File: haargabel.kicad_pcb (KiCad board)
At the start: 4 copper layers, 159 x 36 mm, 95 parts, among them J1 SWD, J2 USB_B_Micro, J3 Conn_01x03, SW1 SKRKAEE020, U1 ATSAML21E15B-MUT, U2 MCP73831-2-OT, U3 TPS79330-EP, U4 MPU-6050, U5 TPS22929D

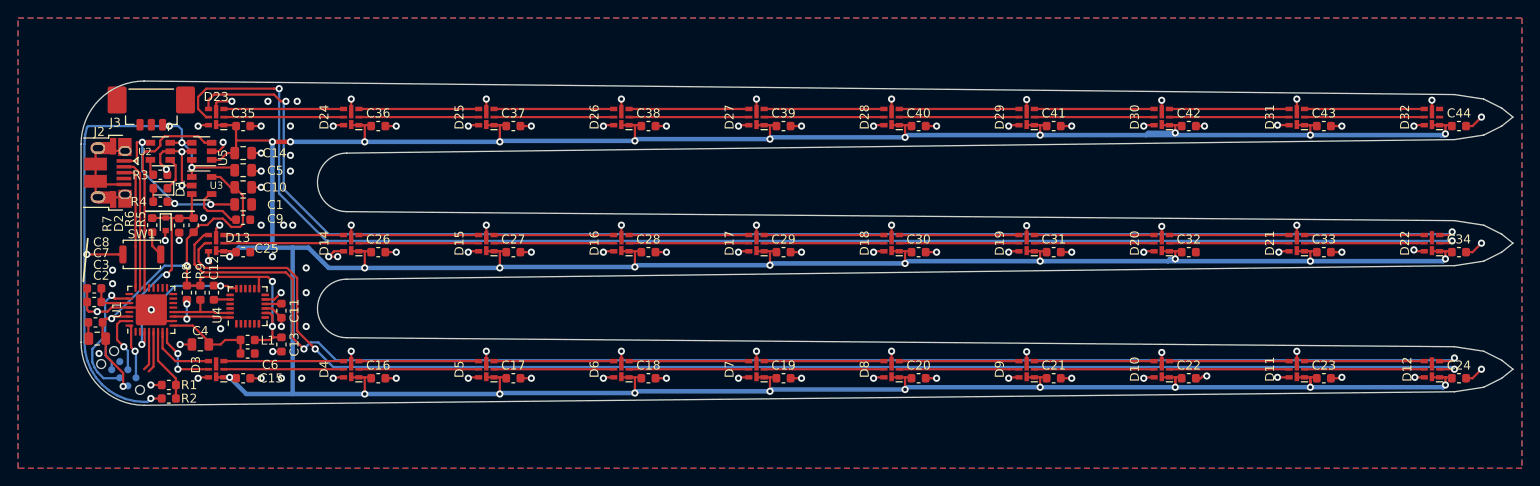
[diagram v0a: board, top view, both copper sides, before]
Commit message: Use a different MCU to make programming easier
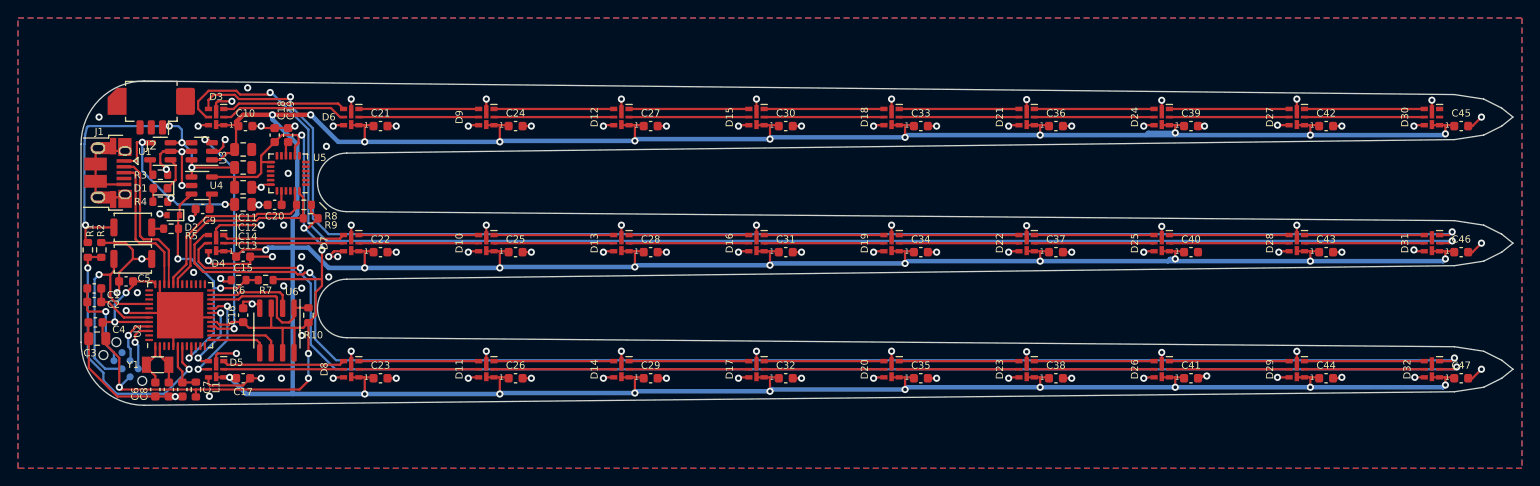
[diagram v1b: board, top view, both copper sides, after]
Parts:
- removed the C4 at (123.2, 79.2)
- removed the U1 at (117.8, 75.4)
- added C16: 100n, Capacitor_SMD:C_0603_1608Metric, F.Cu at (128.0, 76.0)
- added C5: 100n, Capacitor_SMD:C_0603_1608Metric, F.Cu at (115.0, 72.2)
- added C6: 100n, Capacitor_SMD:C_0603_1608Metric, F.Cu at (118.2, 84.2)
- added C8: 100n, Capacitor_SMD:C_0603_1608Metric, F.Cu at (119.8, 84.2)
- added R10: 10k, Resistor_SMD:R_0603_1608Metric, F.Cu at (135.2, 76.0)
- added SW2: SKRKAEE020, Button_Switch_SMD:SW_Push_SPST_NO_Alps_SKRK, F.Cu at (115.8, 69.8)
- added U2: ATSAMD21G18A-M, Package_DFN_QFN:QFN-48-1EP_7x7mm_P0.5mm_EP5.15x5.15mm, F.Cu at (121.0, 76.0)
- added U6: AT25SF081-SSHD-X, Package_SO:SOIC-8_3.9x4.9mm_P1.27mm, F.Cu at (131.8, 77.7)
- added Y1: Crystal, Crystal:Crystal_SMD_3215-2Pin_3.2x1.5mm, F.Cu at (118.5, 81.5)
- J2: renamed from J3; footprint Connector_Molex:Molex_PicoBlade_53398-0371_1x03-1MP_P1.25mm_Vertical -> Connector_Molex:Molex_PicoBlade_53261-0371_1x03-1MP_P1.25mm_Horizontal
- moved C18 23.3 mm to (131.5, 56.0), turned to 90 degrees
- moved C19 19.5 mm to (133.0, 56.0), turned to 90 degrees
- moved R1 18.8 mm to (110.8, 68.8), turned to -90 degrees
- moved R2 16.8 mm to (112.2, 68.8), turned to 90 degrees
- moved R9 16.0 mm to (135.5, 65.2), turned to 180 degrees
- moved U5 15.4 mm to (133.0, 60.2), turned to 180 degrees
- moved R8 15.1 mm to (134.8, 63.8), turned to 180 degrees
- moved C20 11.9 mm to (131.5, 63.8), turned to 180 degrees
- moved R7 10.1 mm to (130.5, 72.1), turned to 180 degrees
- moved R6 8.96 mm to (127.5, 72.1), turned to 180 degrees
- moved C7 8.28 mm to (121.2, 84.2), turned to -90 degrees
- moved L1 7.96 mm to (122.8, 84.2), turned to 90 degrees
- moved C9 4.66 mm to (123.5, 64.2), turned to 0 degrees
- moved SW1 3.16 mm to (115.8, 66.2)
- moved R5 2.14 mm to (120.0, 66.4), turned to 0 degrees
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- renumbered C8 to C1, C35 to C10, C14 to C11, C5 to C12, C1 to C13, C10 to C14, C25 to C15, C15 to C17, C13 to C18, C11 to C19, C7 to C2, C12 to C20, C36 to C21, C26 to C22, C16 to C23, C37 to C24, C27 to C25, C17 to C26, C38 to C27, C18 to C29, C2 to C3, C39 to C30, C29 to C31, C19 to C32, C40 to C33, C30 to C34, C20 to C35, C41 to C36, C31 to C37, C21 to C38, C42 to C39, C3 to C4, C32 to C40, C22 to C41, C43 to C42, C33 to C43, C23 to C44, C44 to C45, C34 to C46, C24 to C47, C6 to C7, D15 to D10, D5 to D11, D26 to D12, D16 to D13, D6 to D14, D27 to D15, D17 to D16, D7 to D17, D28 to D18, D18 to D19, D8 to D20, D29 to D21, D19 to D22, D9 to D23, D30 to D24, D20 to D25, D10 to D26, D31 to D27, D21 to D28, D11 to D29, D23 to D3, D32 to D30, D22 to D31, D12 to D32, D13 to D4, D3 to D5, D24 to D6, D14 to D7, D4 to D8, D25 to D9, J2 to J1, J1 to J3, R7 to R5, R5 to R7, R9 to R8, R8 to R9, U2 to U1, U5 to U3, U3 to U4, U4 to U5
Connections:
- net /EN renamed /PWR_ON
- net /led10_2/CKI renamed /led10_1/CKO
- net /led10_2/SDI renamed /led10_1/SDO
- net /led10_3/CKI renamed /led10_2/CKO
- net /led10_3/SDI renamed /led10_2/SDO
- D30 pad 2: (no net) -> /led10_3/CKO
- D30 pad 3: (no net) -> /led10_3/SDO
- J1 pad 4: (no net) -> unconnected-(J1-Pad4)
- J2 pad 2: (no net) -> unconnected-(J2-Pad2)
- J3 pad 6: (no net) -> unconnected-(J3-Pad6)
- U5 pad 12: (no net) -> unconnected-(U5-Pad12)
- U5 pad 6: (no net) -> unconnected-(U5-Pad6)
- U5 pad 7: (no net) -> unconnected-(U5-Pad7)
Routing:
- net +3V0: track 67.0 -> 120.2 mm, vias 5 -> 8
- net GND: track 185.4 -> 226.8 mm, vias 122 -> 117
- net +BATT: track 66.3 -> 40.9 mm, vias 5 -> 4
- net /BAT_SENSE: track 8.24 -> 30.1 mm, vias 0 -> 2
- net /FLASH_~{CS}: track 0.00 -> 15.1 mm
- net /MPU_SDA: track 8.77 -> 22.4 mm, vias 2 -> 0
- net /MPU_SCL: track 7.72 -> 21.1 mm
- net /FLASH_MISO: track 0.00 -> 9.21 mm
- net (no net): track 9.03 -> 0.00 mm
- net /nRESET: track 14.4 -> 23.3 mm
- net /FLASH_SCK: track 0.00 -> 7.79 mm
- net /FLASH_MOSI: track 0.00 -> 6.63 mm
- net /X32_0: track 0.00 -> 4.62 mm
- net /PWR_ON: track 24.5 -> 29.1 mm, vias 2 -> 3
- net VDDA: track 10.2 -> 5.73 mm
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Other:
- copper layers 4 -> 2
- net class Default removed
- rule pad_to_mask_clearance: 0.051 -> 0
- board text added: "r03"
- board text removed: "+"
- board text removed: "connect here"
- board text removed: "r01"

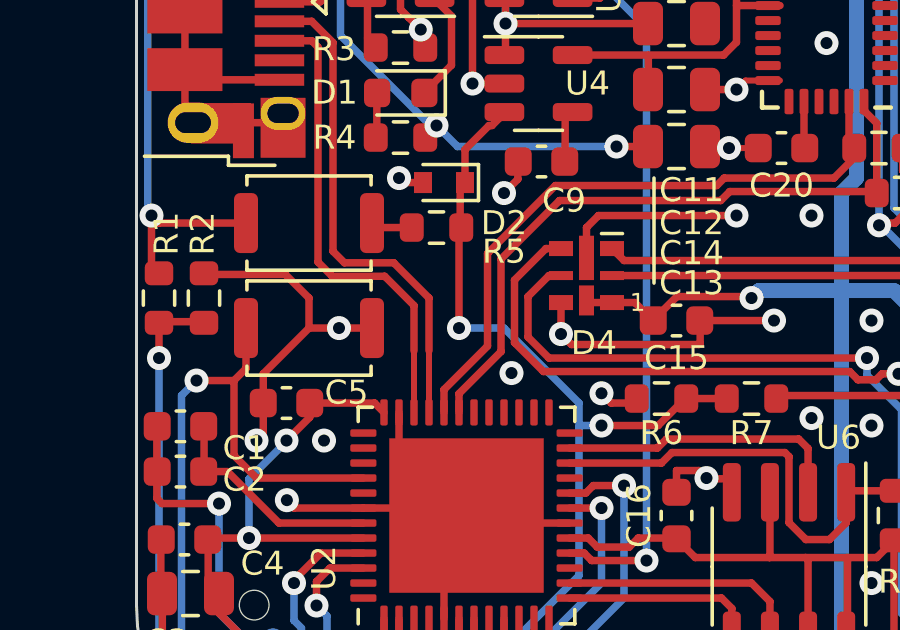
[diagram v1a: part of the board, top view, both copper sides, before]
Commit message: Add Silkscreen for the buttons
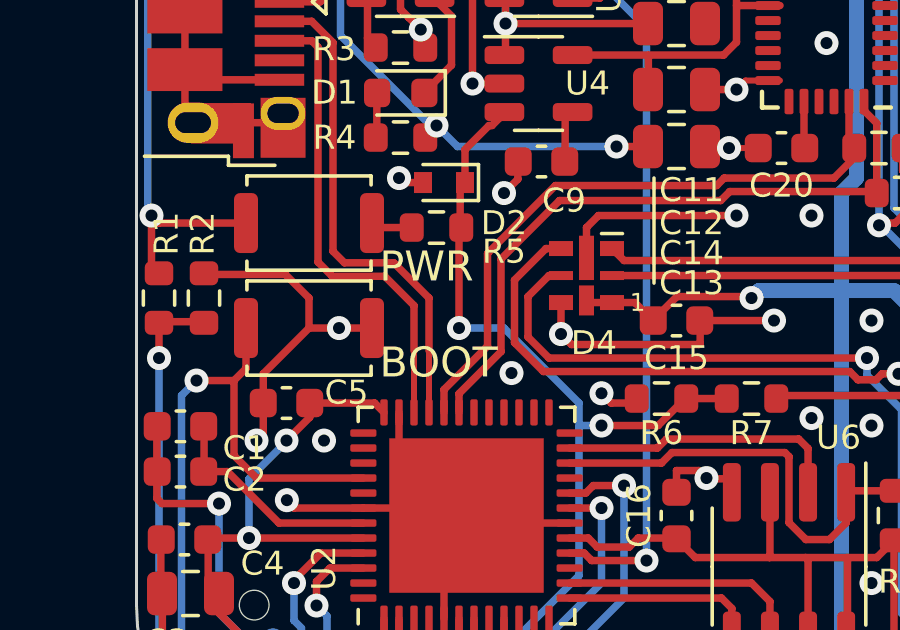
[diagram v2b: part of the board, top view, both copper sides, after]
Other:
- board text added: "BOOT"
- board text added: "PWR"
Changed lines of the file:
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@@
     (effects (font (size 1.5 1.5) (thickness 0.25)) (justify mirror))
+  )
+  (gr_text "PWR" (at 118.1 67.7) (layer "F.SilkS")
+    (effects (font (size 1 1) (thickness 0.2)) (justify left))
+  )
+  (gr_text "BOOT" (at 118.1 70.9) (layer "F.SilkS")
+    (effects (font (size 1 1) (thickness 0.2)) (justify left))
   )
   (gr_text "r03" (at 132.8 69.4) (layer "F.Mask")

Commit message: Simplify component values
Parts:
- C6, C8: value 100n -> 12p
- D1: value LED -> blue
- J2: value Conn_01x03 -> Picoblade_01x03
- R1: value 200k -> 100k
- R3: value 2k -> 4.7k
- R4: value 470R -> 270R
- Y1: value Crystal -> 32kHz
